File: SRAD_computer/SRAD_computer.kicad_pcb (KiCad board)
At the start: 2 copper layers, 56 parts, among them J1 Terminal_3, J2 Conn_01x02, J3 UJ20-C-H-G-SMT-1-P16-TR, J4 Terminal_2, Q1 MMBT5551L, Q3 FDN340P, U1 NCP1117-3.3_SOT223, U2 W25Q128JVS, U3 RP2040, U4 BME280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

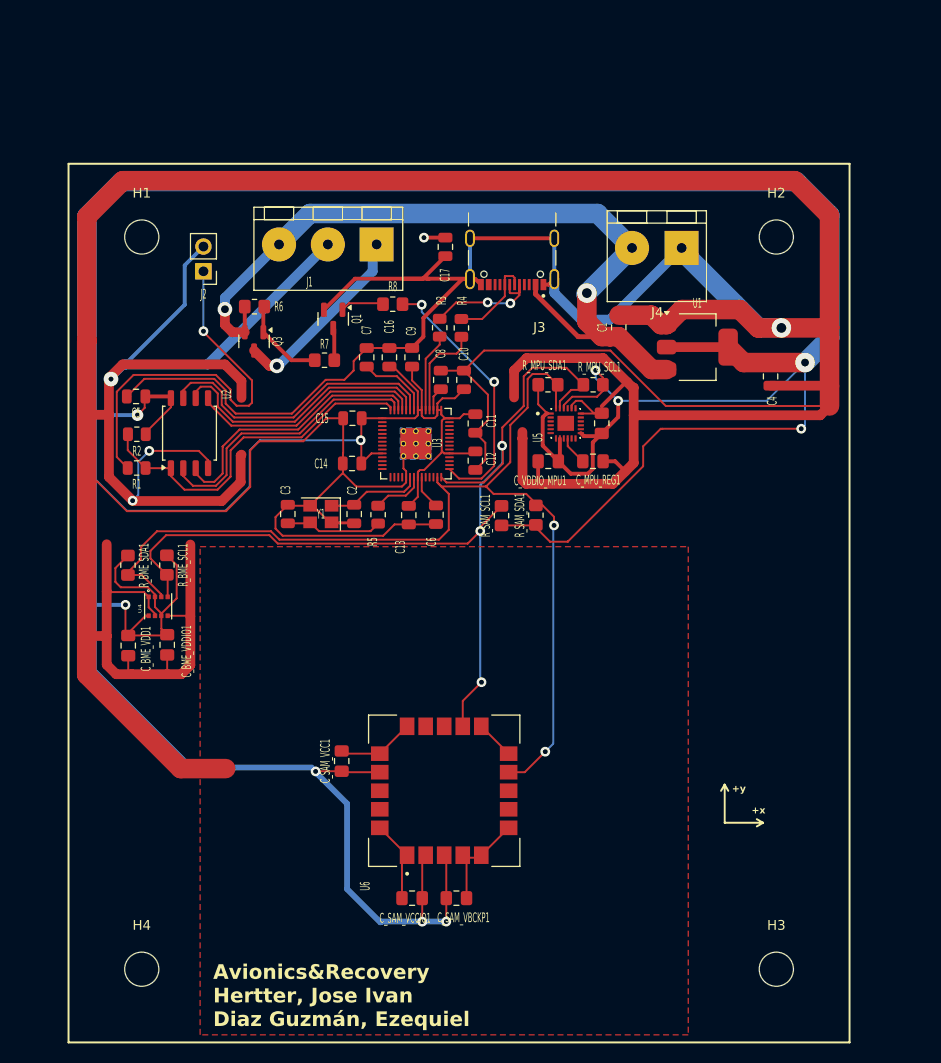
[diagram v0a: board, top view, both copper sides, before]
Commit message: SD slot, LEDs and switch added
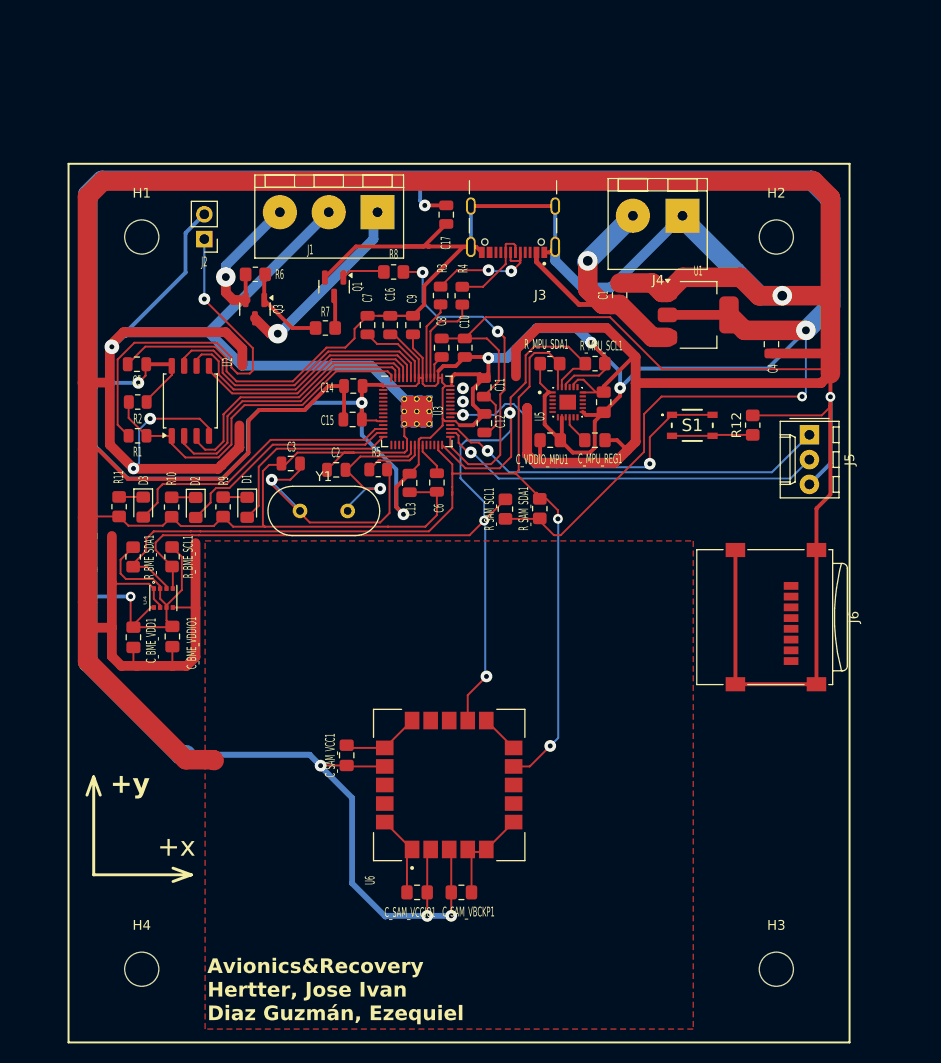
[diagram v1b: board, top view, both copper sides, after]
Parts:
- added D1: LED, LED_SMD:LED_0805_2012Metric_Pad1.15x1.40mm_HandSolder, F.Cu at (68.3, 85.2)
- added D2: LED, LED_SMD:LED_0805_2012Metric_Pad1.15x1.40mm_HandSolder, F.Cu at (63.0, 85.2)
- added D3: LED, LED_SMD:LED_0805_2012Metric_Pad1.15x1.40mm_HandSolder, F.Cu at (57.6, 85.2)
- added J5: Connector_3_Pol, TCLib:Molex_1x03_P2.54mm, F.Cu at (125.9, 77.8)
- added J6: Micro_SD_Card, Connector_Card:microSD_HC_Wuerth_693072010801, F.Cu at (122.5, 96.4)
- added R10: R, TCLib:R_0805, F.Cu at (60.6, 85.2)
- added R11: R, TCLib:R_0805, F.Cu at (55.2, 85.1)
- added R12: R, TCLib:R_0805, F.Cu at (120.1, 76.8)
- added R9: R, Resistor_SMD:R_0805_2012Metric_Pad1.20x1.40mm_HandSolder, F.Cu at (65.8, 85.1)
- added S1: PTS810SJK250SMTR_LFS, Rocketry_FC:PTS810SJK250SMTRLFS, F.Cu at (113.9, 76.8)
- Y1: value ABM8-272-T3 -> Crystal; footprint Crystal:Crystal_SMD_3225-4Pin_3.2x2.5mm -> Crystal:Crystal_HC49-4H_Vertical
- moved C3 5.19 mm to (72.8, 80.7), turned to 180 degrees
- moved C2 4.89 mm to (77.4, 81.3), turned to 180 degrees
- moved R5 4.62 mm to (81.7, 81.3), turned to 0 degrees
- moved C14 4.51 mm to (79.1, 76.2)
- moved C12 3.95 mm to (92.6, 76.6)
- moved C11 3.80 mm to (92.5, 72.9)
- moved C10 3.30 mm to (90.6, 68.8)
- moved C6 3.30 mm to (87.7, 82.6)
- moved J1 3.30 mm to (81.7, 55.0)
- moved U2 3.30 mm to (62.5, 74.3)
- moved C1 3.30 mm to (106.5, 63.5)
- moved C13 3.30 mm to (84.9, 82.7)
- moved C15 3.30 mm to (79.2, 72.8)
- moved C16 3.30 mm to (83.0, 66.5)
- moved C17 3.30 mm to (88.7, 55.2)
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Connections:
- net /GPIO16 renamed /SDA
- net /GPIO17 renamed /SCL
- net /GPIO18 renamed /power_cam
- J1 pad 3: VBUS -> V_cam_bus
- Q3 pad 2: VBUS -> V_cam_bus
- R6 pad 1: VBUS -> V_cam_bus
- U3 pad 12: /GPIO9 -> /LED_3
- U3 pad 13: /GPIO10 -> /LED_2
- U3 pad 14: /GPIO11 -> /LED_1
- U3 pad 30: /GPIO19 -> /UART_Tx
- U3 pad 31: /GPIO20 -> /UART_Rx
- U3 pad 35: /GPIO23 -> /SW_1
- Y1 pad 1: /XIN -> Net-(C3-Pad1)
- Y1 pad 2: GND -> /XIN
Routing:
- net GND: track 720.4 -> 834.7 mm, vias 4 -> 5
- net VBUS: track 85.6 -> 31.1 mm, vias 2 -> 1
- net +3V3: track 470.2 -> 517.4 mm, vias 11 -> 13
- net /UART_Rx: track 0.00 -> 40.2 mm, vias 0 -> 1
- net /UART_Tx: track 0.00 -> 40.0 mm, vias 0 -> 1
- net /SW_1: track 0.00 -> 36.5 mm, vias 0 -> 2
- net /LED_3: track 0.00 -> 29.1 mm
- net /LED_2: track 0.00 -> 23.3 mm
- net /LED_1: track 0.00 -> 19.7 mm
- net Net-(C3-Pad1): track 9.99 -> 28.0 mm, vias 0 -> 1
- net V_cam_bus: track 0.00 -> 15.5 mm, vias 0 -> 1
- net Net-(S1-COM_1): track 0.00 -> 8.30 mm
- net /SCL: track 103.2 -> 111.2 mm
- net /XIN: track 9.79 -> 17.0 mm, vias 0 -> 1
- net /power_cam: track 27.6 -> 34.4 mm
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
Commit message: PCB_V1 finished
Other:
- board text added: "A&R Hertter, Jose Ivan Diaz Guzmán, Ezequiel"
- board text removed: "Avionics&Recovery Hertter, Jose Ivan Diaz Guzmán, Ezequiel"

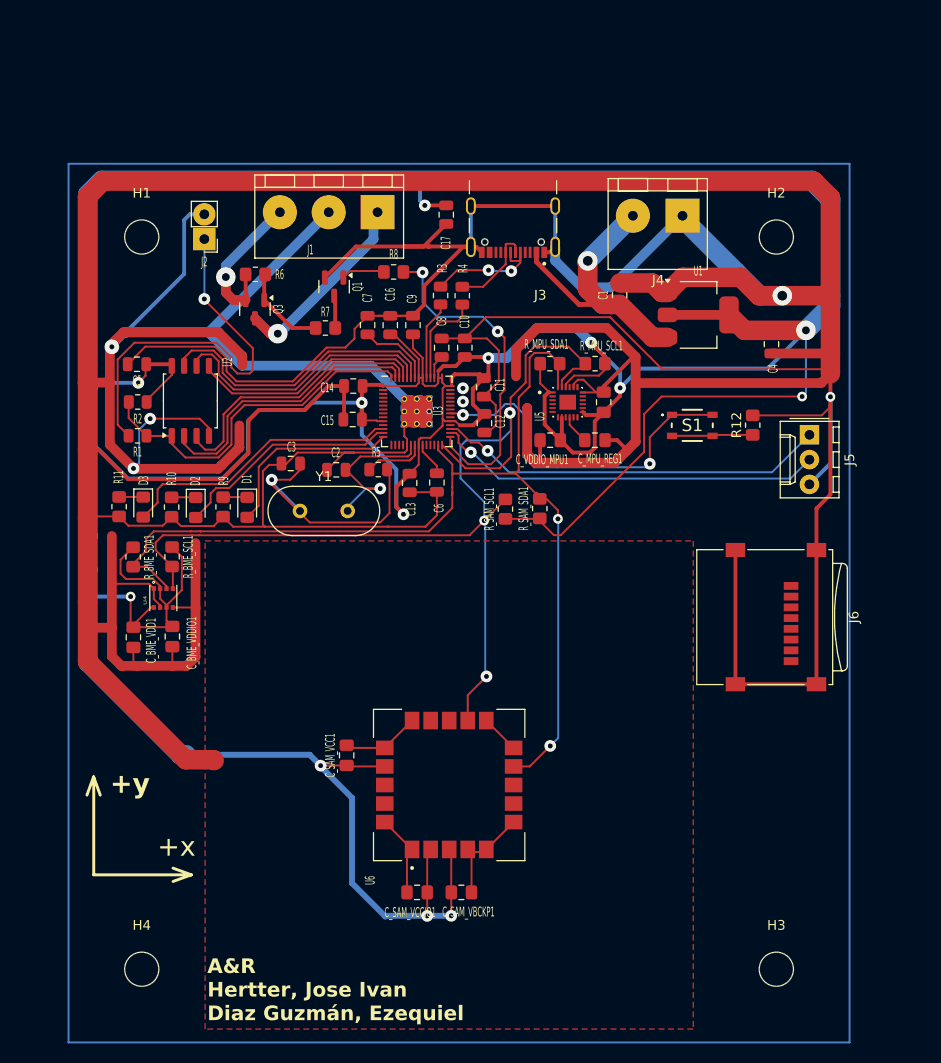
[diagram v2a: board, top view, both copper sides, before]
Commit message: PCB 3D model added
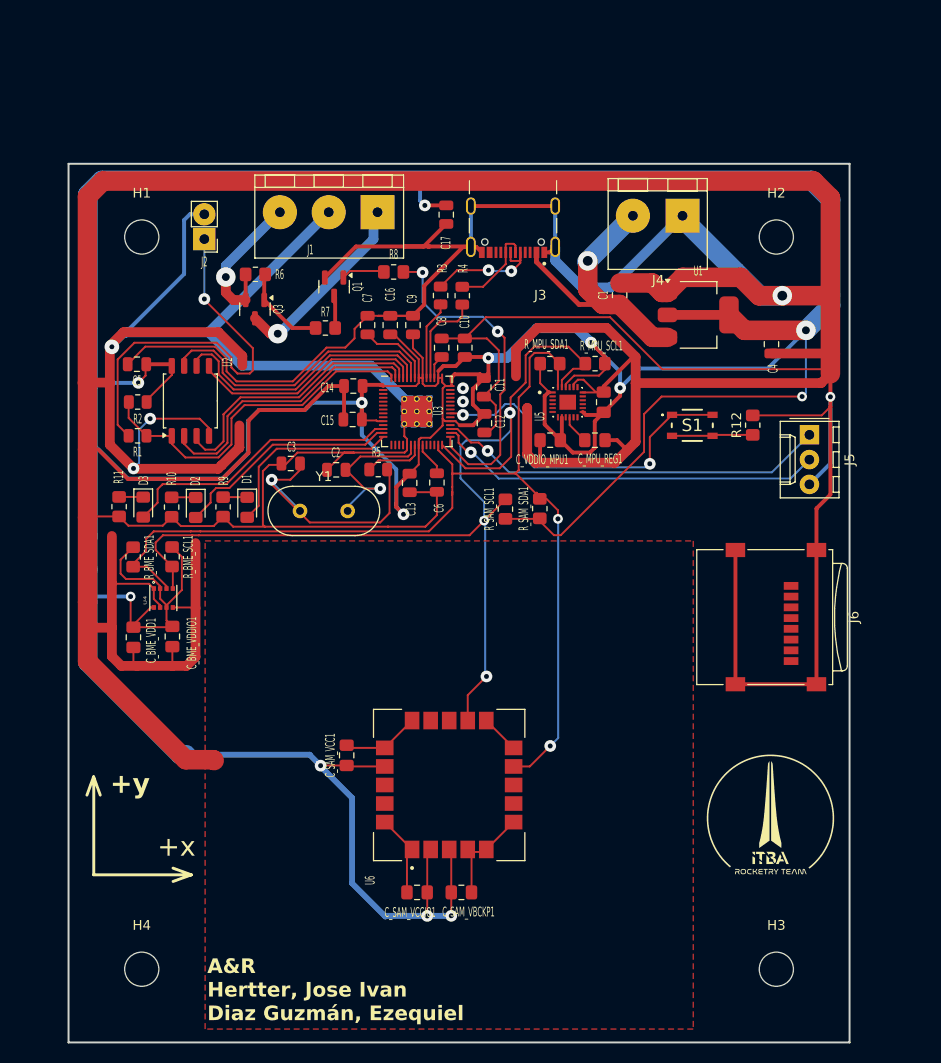
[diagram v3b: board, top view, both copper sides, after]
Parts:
- added G***: LOGO, my_lib:Logo_ITBA_rocketry, F.Cu at (121.9, 117.2)
- J6: footprint Connector_Card:microSD_HC_Wuerth_693072010801 -> my_lib:microSD_HC_Wuerth_693072010801
- S1: footprint Rocketry_FC:PTS810SJK250SMTRLFS -> my_lib:PTS810SJK250SMTRLFS
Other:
- board outline added: 80 x 90 mm

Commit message: PCB V2 first draft
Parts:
- J6: footprint my_lib:microSD_HC_Wuerth_693072010801 -> my_lib:microSD_HC_Molex_47219-2001
- S1: footprint my_lib:PTS810SJK250SMTRLFS -> Rocketry_FC:PTS810SJK250SMTRLFS
- moved R_SAM_SDA1 5.31 mm to (93.0, 86.0)
- moved R12 4.57 mm to (119.6, 81.3), turned to 0 degrees
- moved R_MPU_SDA1 4.48 mm to (102.7, 73.5), turned to 180 degrees
- moved R_SAM_SCL1 4.40 mm to (90.4, 86.0)
- moved C_VDD_MPU1 4.20 mm to (107.8, 77.4)
- moved U5 4.20 mm to (104.1, 77.4)
- moved C_MPU_REG1 4.20 mm to (106.9, 81.3)
- moved C_VDDIO_MPU1 4.20 mm to (102.3, 81.3)
- moved R_MPU_SCL1 4.20 mm to (106.9, 73.5)
- moved S1 3.69 mm to (117.5, 75.9)
- moved C11 2.05 mm to (93.6, 71.2), turned to 0 degrees
- moved C7 1.68 mm to (79.0, 66.5)
- moved C14 1.57 mm to (77.9, 77.2)
- moved C16 1.36 mm to (81.6, 66.5)
- moved C15 1.29 mm to (77.9, 72.5)
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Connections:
- J6 pad 1: unconnected-(J6-DAT2-Pad1) -> /SD_DAT2
- J6 pad 2: unconnected-(J6-DAT3/CD-Pad2) -> /SD_DAT3
- J6 pad 3: unconnected-(J6-CMD-Pad3) -> /SD_CMD
- J6 pad 5: unconnected-(J6-CLK-Pad5) -> /SD_CLK
- J6 pad 6: unconnected-(J6-VSS-Pad6) -> /SD_VSS
- J6 pad 7: unconnected-(J6-DAT0-Pad7) -> /SD_DAT0
- J6 pad 8: unconnected-(J6-DAT1-Pad8) -> /SD_DAT1
- U3 pad 29: /power_cam -> /SD_DAT1
- U3 pad 30: /UART_Tx -> /SD_DAT0
- U3 pad 31: /UART_Rx -> /SD_VSS
- U3 pad 32: /GPIO21 -> /SD_CLK
- U3 pad 34: /GPIO22 -> /SD_CMD
- U3 pad 35: /SW_1 -> /SD_DAT3
- U3 pad 37: /GPIO25 -> /SD_DAT2
- U3 pad 38: /GPIO26_ADC0 -> /UART_Tx
- U3 pad 39: /GPIO27_ADC1 -> /UART_Rx
- U3 pad 40: /GPIO28_ADC2 -> /SW_1
- U3 pad 41: /GPIO29_ADC3 -> /power_cam
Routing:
- net /SD_CMD: track 0.00 -> 52.9 mm
- net /SD_DAT3: track 0.00 -> 52.3 mm
- net /SD_DAT2: track 0.00 -> 51.6 mm
- net /SD_DAT1: track 0.00 -> 51.0 mm
- net /SD_DAT0: track 0.00 -> 50.4 mm
- net /SD_VSS: track 0.00 -> 49.8 mm
- net /SD_CLK: track 0.00 -> 49.1 mm
- net +3V3: track 517.4 -> 548.7 mm, vias 13 -> 15
- net /power_cam: track 34.4 -> 16.8 mm
- net GND: track 835.1 -> 847.5 mm, vias 5 -> 6
- net /SCL: track 111.2 -> 99.5 mm, vias 3 -> 5
- net /SW_1: track 36.5 -> 47.5 mm, vias 2 -> 0
- net /UART_Rx: track 40.2 -> 50.3 mm
- net /UART_Tx: track 40.0 -> 49.5 mm
- net /V_cam: track 19.7 -> 21.8 mm
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
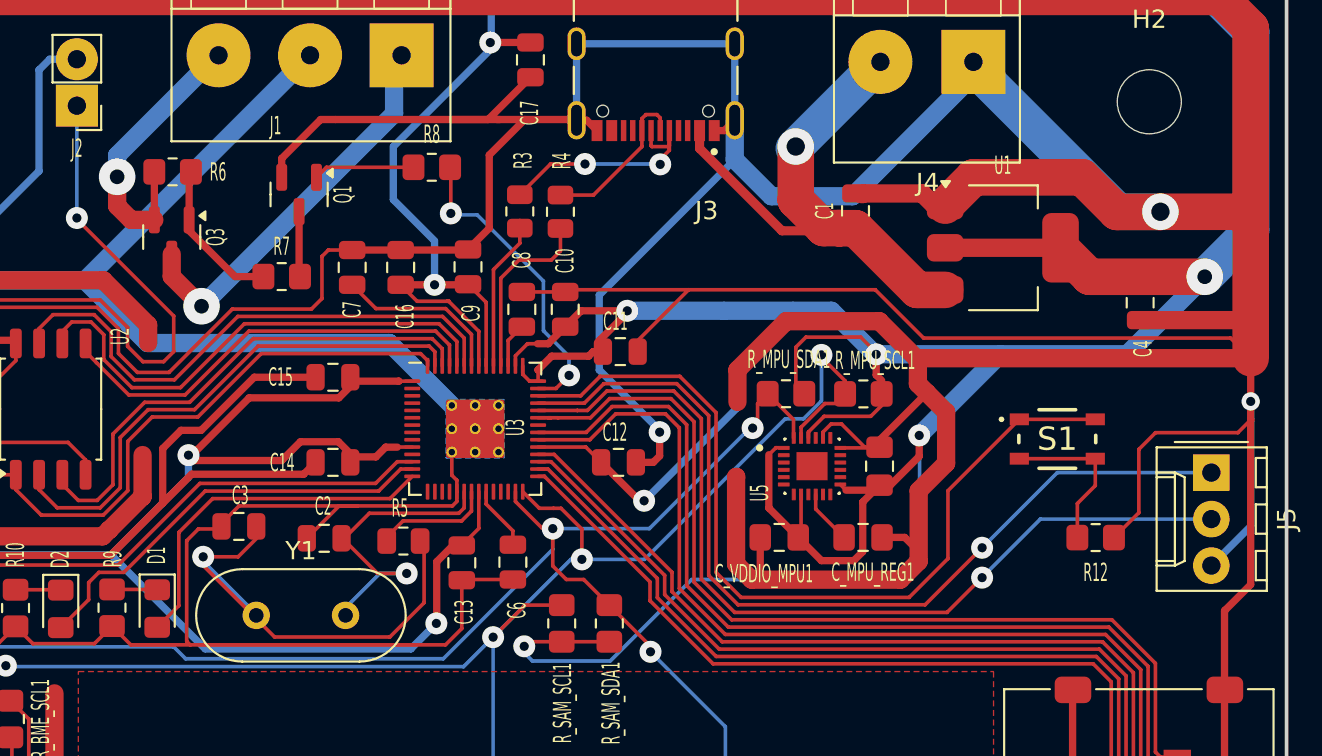
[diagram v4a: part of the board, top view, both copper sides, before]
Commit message: changes in USB pins. D+ -> D-
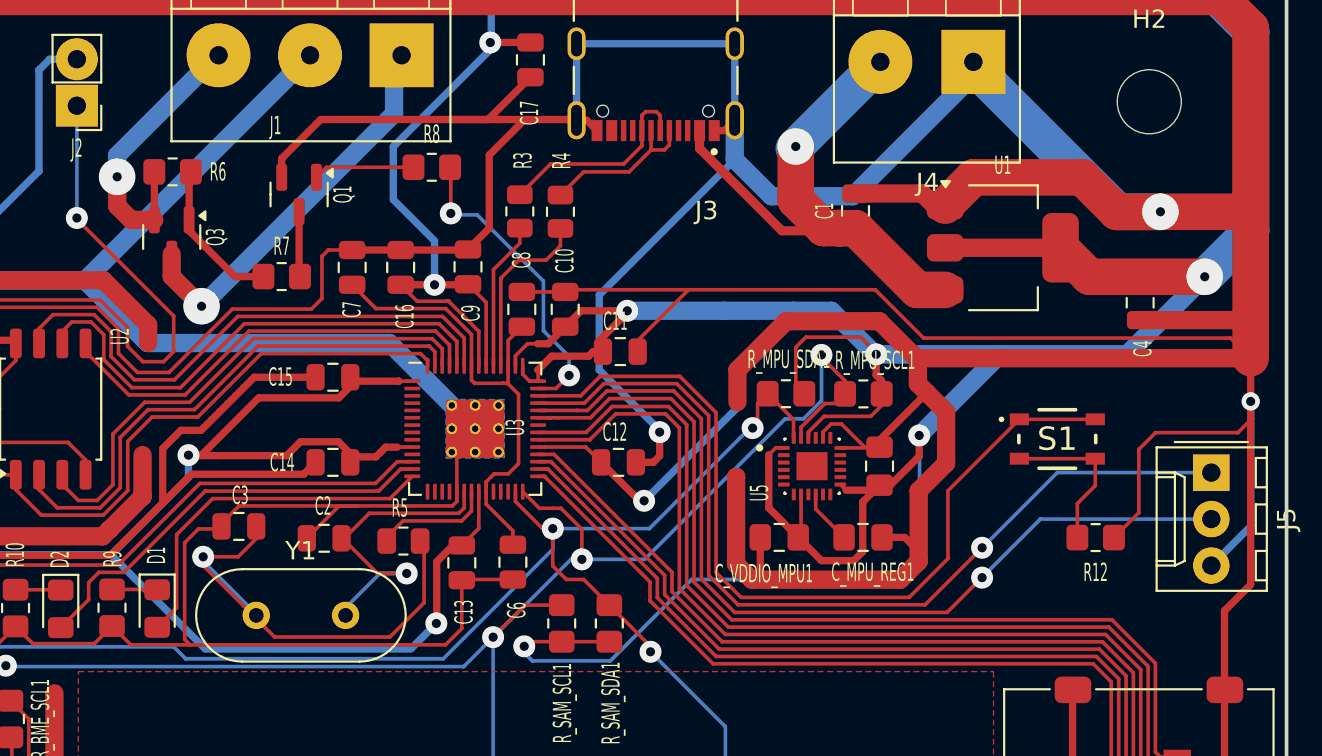
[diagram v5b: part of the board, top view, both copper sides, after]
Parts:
- S1: footprint Rocketry_FC:PTS810SJK250SMTRLFS -> my_lib:PTS810SJK250SMTRLFS
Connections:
- J3 pad A6: /USB_D- -> /USB_D+
- J3 pad A7: /USB_D+ -> /USB_D-
- J3 pad B6: /USB_D- -> /USB_D+
- J3 pad B7: /USB_D+ -> /USB_D-
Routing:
- net +1V1: track 15.3 -> 26.5 mm
- net /USB_D+: track 13.1 -> 11.4 mm, vias 2 -> 0

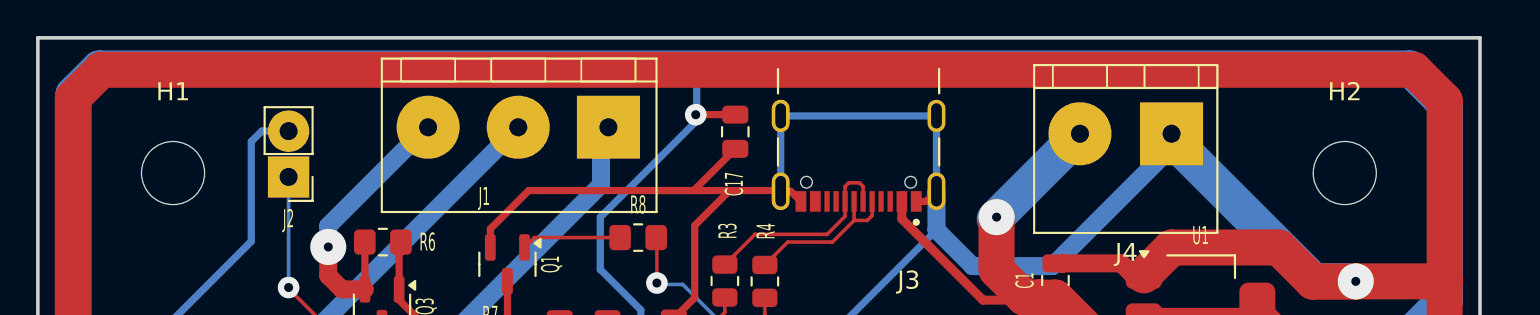
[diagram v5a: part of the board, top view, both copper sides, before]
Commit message: USB gnd fixed
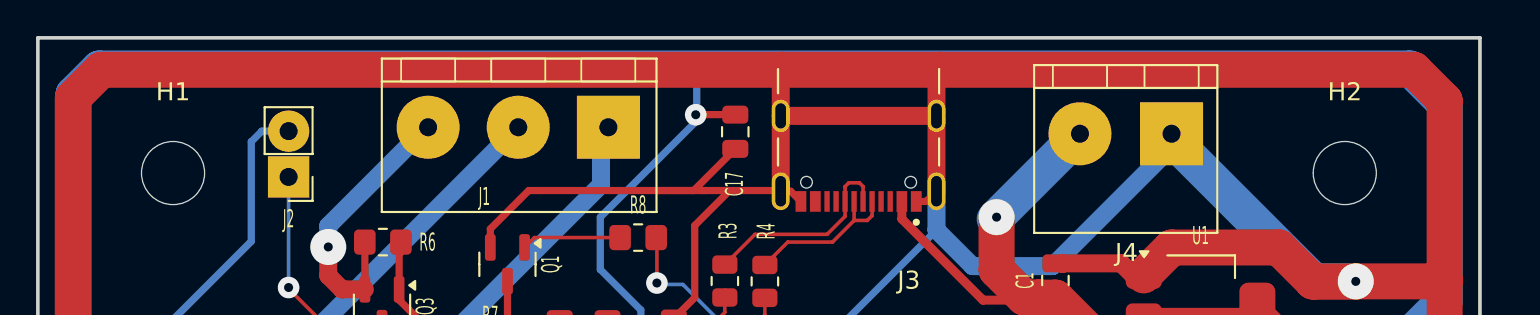
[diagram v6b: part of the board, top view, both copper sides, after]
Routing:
- net GND: track 847.5 -> 852.7 mm

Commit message: SD layout
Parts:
- added C18: 10u, TCLib:C_0805, F.Cu at (93.8, 117.9)
- added R13: R, TCLib:R_0805, F.Cu at (93.8, 110.9)
- added R14: 10k, TCLib:R_0805, F.Cu at (93.8, 114.4)
- added R15: 10k, TCLib:R_0805, F.Cu at (93.9, 120.6)
- moved H4 81.7 mm to (52.6, 50.9), turned to -90 degrees
- moved H3 71.9 mm to (52.6, 115.9), turned to -90 degrees
- moved H1 70.4 mm to (127.6, 50.9), turned to -90 degrees
- moved J2 63.5 mm to (127.4, 57.4), turned to 90 degrees
- moved C5 60.9 mm to (114.5, 50.5), turned to 90 degrees
- moved R2 58.7 mm to (110.7, 50.5), turned to 90 degrees
- moved H2 58.7 mm to (127.6, 115.9), turned to -90 degrees
- moved R11 57.8 mm to (100.0, 48.6), turned to 180 degrees
- moved C_BME_VDD1 57.7 mm to (85.6, 49.8), turned to 180 degrees
- moved R1 57.1 mm to (107.2, 50.5), turned to 90 degrees
- moved R_BME_SDA1 56.0 mm to (93.8, 49.7), turned to 180 degrees
- moved G*** 55.8 mm to (66.2, 115.7)
- moved R6 54.6 mm to (123.8, 62.6), turned to -90 degrees
- moved D3 54.3 mm to (99.9, 51.1), turned to 180 degrees
- moved J4 53.7 mm to (129.8, 106.3), turned to 90 degrees
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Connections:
- J6 pad 4: unconnected-(J6-VDD-Pad4) -> +3V3
- J6 pad 6: /SD_VSS -> GND
- U3 pad 29: /SD_DAT1 -> /GPIO18
- U3 pad 31: /SD_VSS -> /SD_CLK
- U3 pad 32: /SD_CLK -> /SD_CMD
- U3 pad 34: /SD_CMD -> /SD_DAT3
- U3 pad 35: /SD_DAT3 -> /SD_DAT2
- U3 pad 37: /SD_DAT2 -> /SD_DAT1
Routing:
- net GND: track 852.7 -> 945.8 mm, vias 6 -> 185
- net /SD_VSS: track 49.8 -> 0.00 mm
- net +3V3: track 548.5 -> 589.6 mm, vias 15 -> 16
- net /SD_DAT1: track 51.0 -> 72.8 mm
- net /SD_DAT0: track 50.4 -> 55.9 mm
- net /SD_DAT3: track 52.3 -> 56.8 mm
- net /SD_DAT2: track 51.6 -> 55.3 mm
- net /SD_CLK: track 49.1 -> 51.8 mm
- net /power_cam: track 16.8 -> 19.4 mm
- net /SD_CMD: track 52.9 -> 50.9 mm
- net /USB_D-: track 8.92 -> 10.7 mm
- net Net-(U3-USB_DP): track 8.54 -> 6.93 mm
- net Net-(U3-USB_DM): track 9.73 -> 8.44 mm
- net /USB_D+: track 11.4 -> 12.5 mm
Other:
- board size 80 x 90 mm -> 90 x 80 mm
